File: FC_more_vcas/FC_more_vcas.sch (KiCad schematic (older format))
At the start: 33 parts, among them J1 Con_Bottom, J2 Con_Top, Q1 Q_PNP_EBC, Q2 Q_PNP_EBC, U1 LM13700

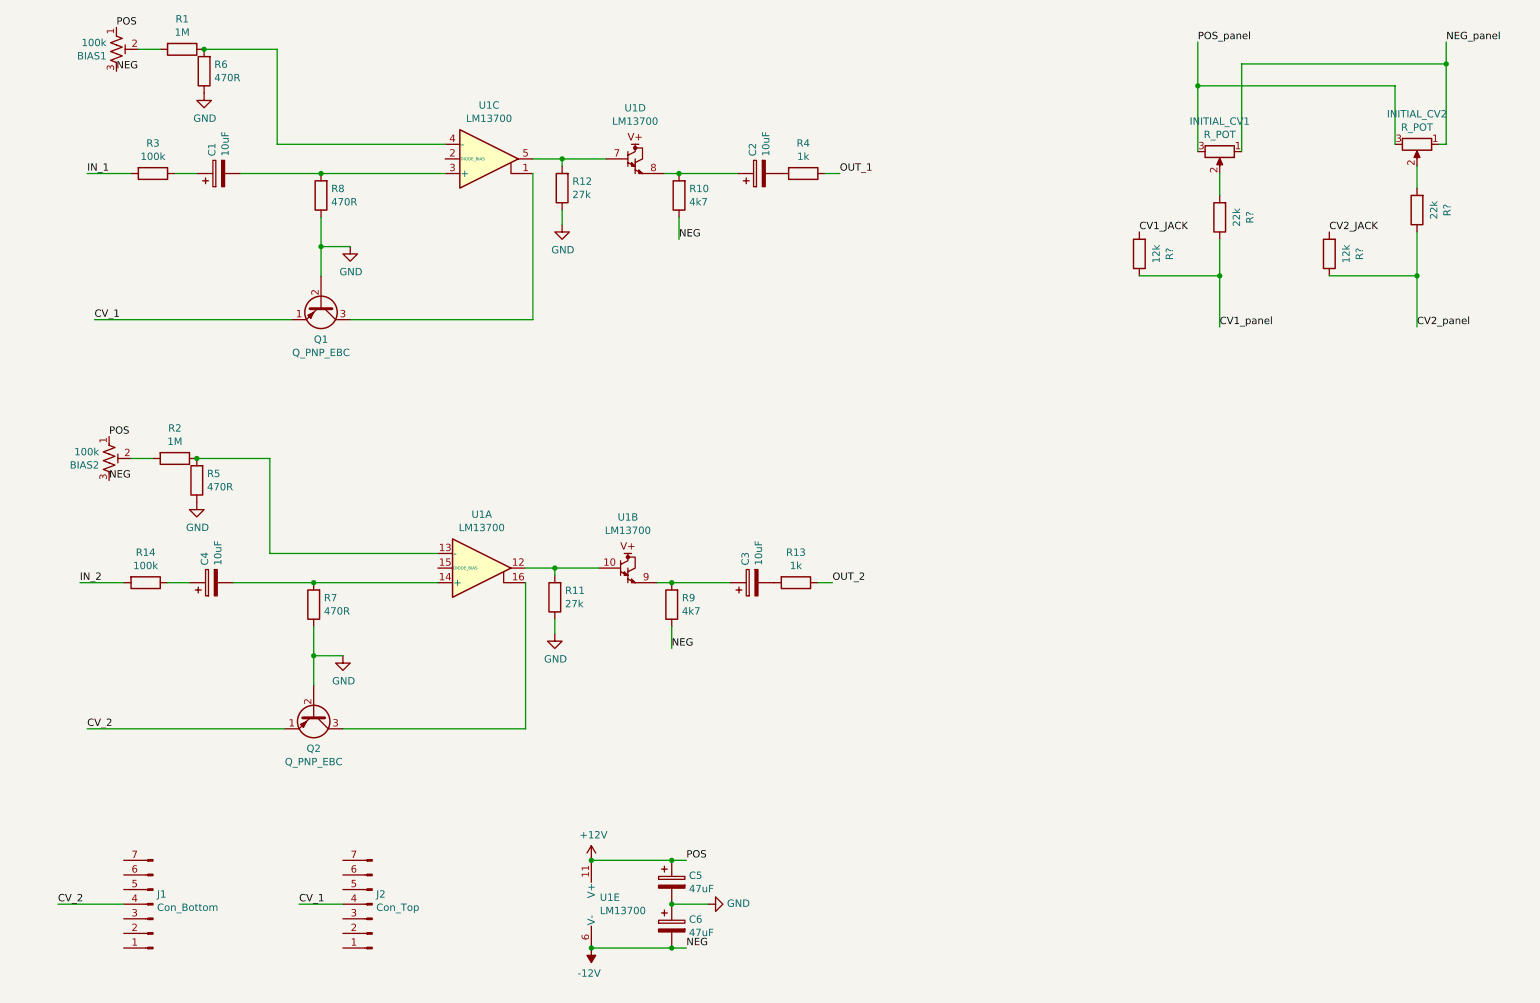
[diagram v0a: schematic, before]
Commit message: Yousynth ADSR layed out in Kicad, WASP reworked for more compact layout, FC more VCAs layed out
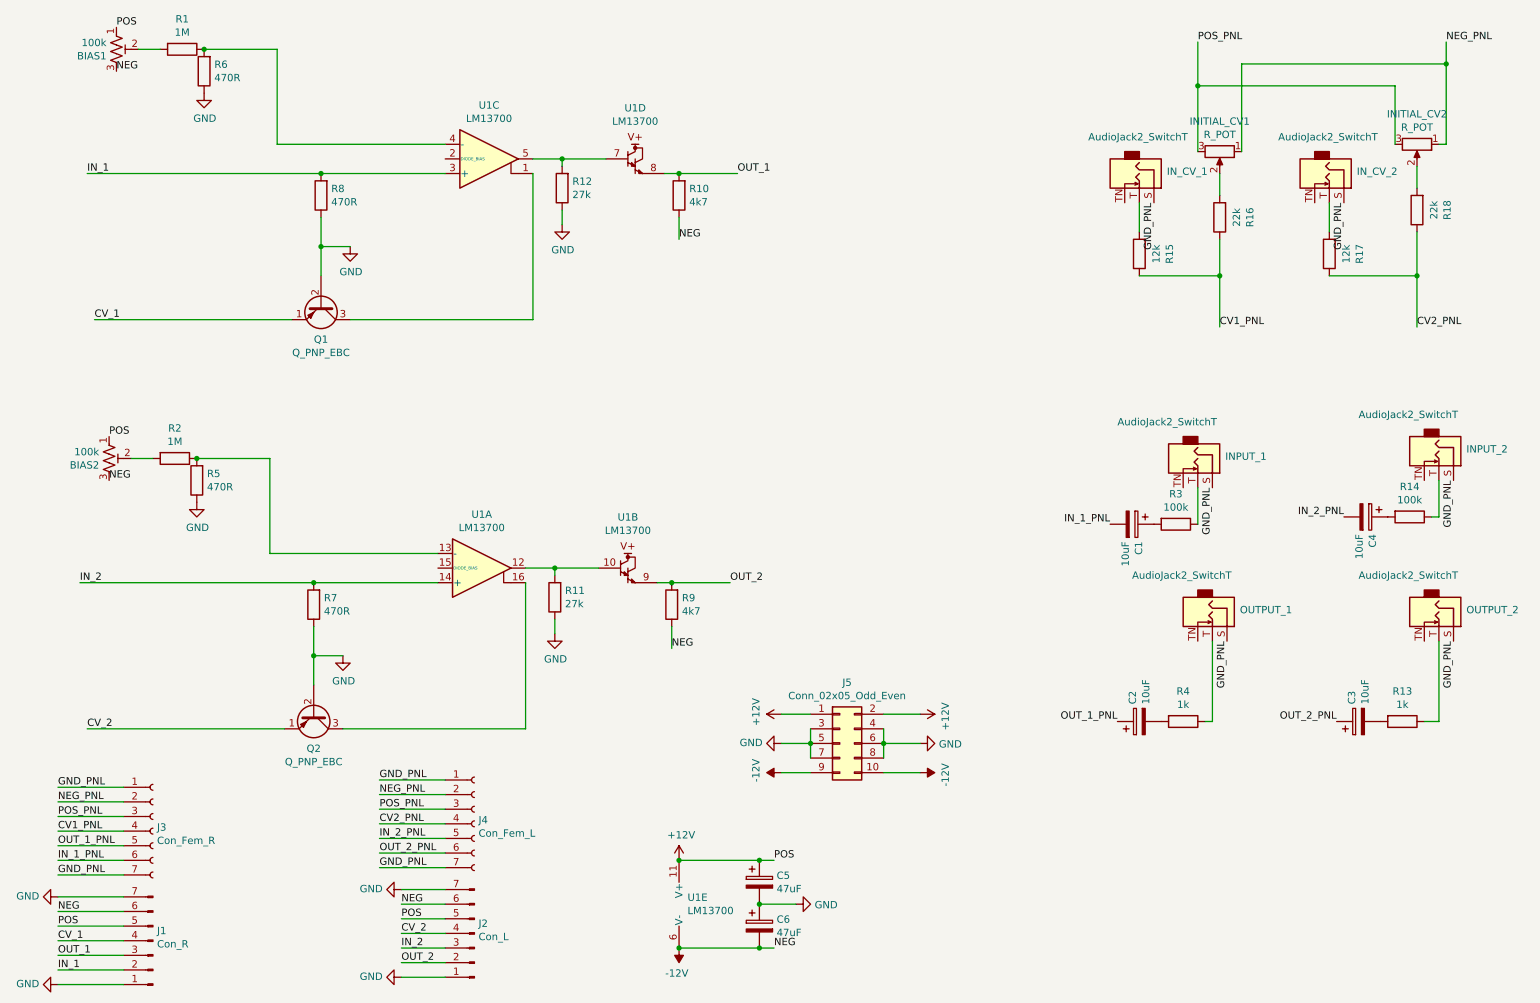
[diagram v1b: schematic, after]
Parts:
- added INPUT_1, INPUT_2, IN_CV_1, IN_CV_2, OUTPUT_1, OUTPUT_2: AudioJack2_SwitchT, Connector_Audio:Jack_3.5mm_QingPu_WQP-PJ398SM_Vertical_CircularHoles, symbol Connector:AudioJack2_SwitchT
- added J3: Con_Fem_R, Connector_PinSocket_2.54mm:PinSocket_1x07_P2.54mm_Vertical, symbol Connector:Conn_01x07_Female
- added J4: Con_Fem_L, Connector_PinSocket_2.54mm:PinSocket_1x07_P2.54mm_Vertical, symbol Connector:Conn_01x07_Female
- added J5: Conn_02x05_Odd_Even, Connector_PinHeader_2.54mm:PinHeader_2x05_P2.54mm_Vertical, symbol Connector_Generic:Conn_02x05_Odd_Even
- BIAS1, BIAS2: footprint (none) -> Potentiometer_THT:Potentiometer_Bourns_3296W_Vertical
- C1, C2, C3, C4: footprint (none) -> Capacitor_THT:CP_Radial_D5.0mm_P2.50mm
- C5, C6: footprint (none) -> Capacitor_THT:CP_Radial_D6.3mm_P2.50mm
- INITIAL_CV1, INITIAL_CV2: footprint (none) -> Potentiometer_THT:Potentiometer_Alpha_RD901F-40-00D_Single_Vertical
- J1: value Con_Bottom -> Con_R; footprint (none) -> Connector_PinHeader_2.54mm:PinHeader_1x07_P2.54mm_Vertical
- J2: value Con_Top -> Con_L; footprint (none) -> Connector_PinHeader_2.54mm:PinHeader_1x07_P2.54mm_Vertical
- Q1, Q2: footprint (none) -> Package_TO_SOT_SMD:SOT-23
- R1, R10, R11, R12, R13, R14, R2, R3, R4, R5, R6, R7, R8, R9: footprint (none) -> Resistor_SMD:R_0805_2012Metric_Pad1.15x1.40mm_HandSolder
- R15, R16, R17, R18: renamed from R?; footprint (none) -> Resistor_SMD:R_0805_2012Metric_Pad1.15x1.40mm_HandSolder
- U1: footprint (none) -> Package_DIP:DIP-16_W7.62mm_Socket_LongPads
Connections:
- net +12V: now also J1.5 (Pin_5), J2.5 (Pin_5), J5.1 (Pin_1), J5.2 (Pin_2)
- net -12V: now also J1.6 (Pin_6), J2.6 (Pin_6), J5.10 (Pin_10), J5.9 (Pin_9)
- net CV_1: now also J1.4 (Pin_4); no longer J2.4 (Pin_4)
- net CV_2: now also J2.4 (Pin_4); no longer J1.4 (Pin_4)
- net GND: now also J1.1 (Pin_1), J1.7 (Pin_7), J2.1 (Pin_1), J2.7 (Pin_7), J5.3 (Pin_3), J5.4 (Pin_4), J5.5 (Pin_5), J5.6 (Pin_6), J5.7 (Pin_7), J5.8 (Pin_8)
- net IN_1: now also J1.2 (Pin_2), R8.2, U1.3 (+); no longer R3.2
- net IN_2: now also J2.3 (Pin_3), R7.2, U1.14 (+); no longer R14.2
- net OUT_1: now also J1.3 (Pin_3), R10.2, U1.8; no longer R4.1
- net OUT_2: now also J2.2 (Pin_2), R9.2, U1.9; no longer R13.1
- net at R14.1: now also INPUT_2.T; no longer C4.1
- net at R3.1: now also INPUT_1.T; no longer C1.1
- net CV1_JACK: no longer names the net of R15.2
- net CV1_JACK: now also IN_CV_1.T
- net CV1_panel renamed CV1_PNL
- net CV1_PNL: now also J3.4 (Pin_4)
- net CV2_JACK: no longer names the net of R17.2
- net CV2_JACK: now also IN_CV_2.T
- net CV2_panel renamed CV2_PNL
- net CV2_PNL: now also J4.4 (Pin_4)
- net NEG_panel renamed NEG_PNL
- net NEG_PNL: now also J3.2 (Pin_2), J4.2 (Pin_2)
- net POS_panel renamed POS_PNL
- net POS_PNL: now also J3.3 (Pin_3), J4.3 (Pin_3)
- new net: C4.1, R14.2
- new net: OUTPUT_2.T, R13.1
- new net: C1.1, R3.2
- new net: OUTPUT_1.T, R4.1
- new net GND_PNL: INPUT_1.S, INPUT_2.S, IN_CV_1.S, IN_CV_2.S, J3.1 (Pin_1), J3.7 (Pin_7), J4.1 (Pin_1), J4.7 (Pin_7), OUTPUT_1.S, OUTPUT_2.S
- new net IN_1_PNL: C1.2, J3.6 (Pin_6)
- new net IN_2_PNL: C4.2, J4.5 (Pin_5)
- new net OUT_1_PNL: C2.1, J3.5 (Pin_5)
- new net OUT_2_PNL: C3.1, J4.6 (Pin_6)
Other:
- moved on the sheet: C1, C2, C3, C4, C5, C6, J1, J2, R13, R14, R3, R4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

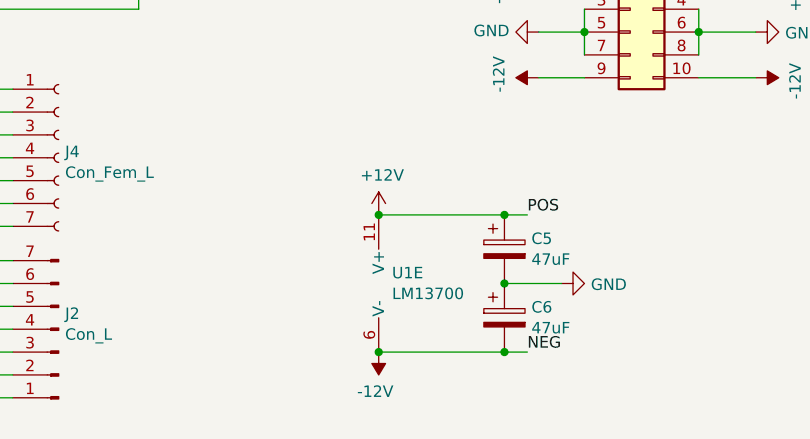
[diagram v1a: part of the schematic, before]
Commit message: Corrections made to ground planes, trace widths, etc. after visual checks of printout
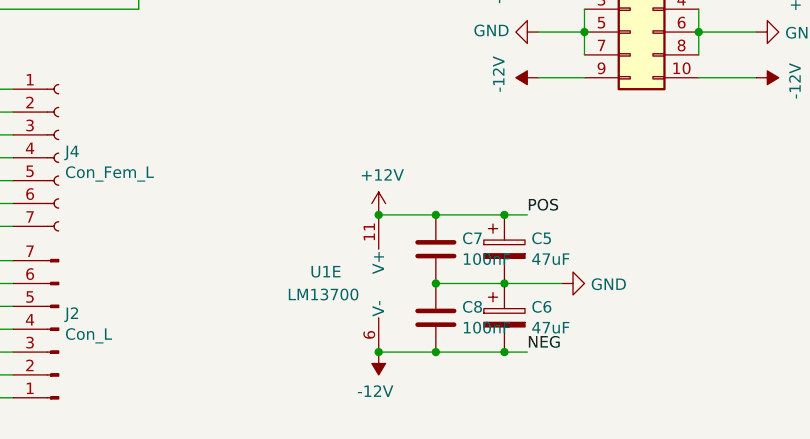
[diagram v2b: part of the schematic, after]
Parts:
- added C7, C8: 100nF, Capacitor_SMD:C_0805_2012Metric_Pad1.15x1.40mm_HandSolder, symbol Device:C
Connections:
- net +12V: now also C7.1
- net -12V: now also C8.2
- net GND: now also C7.2, C8.1
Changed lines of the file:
@@
 U 5 1 5E74031E
 P 5250 6950
-F 0 "U1" H 5208 6996 50  0000 L CNN
-F 1 "LM13700" H 5208 6905 50  0000 L CNN
+F 0 "U1" H 4850 7000 50  0000 L CNN
+F 1 "LM13700" H 4750 6900 50  0000 L CNN
 F 2 "Package_DIP:DIP-16_W7.62mm_Socket_LongPads" H 4950 6975 50  0001 C CNN
 F 3 "http://www.ti.com/lit/ds/symlink/lm13700.pdf" H 4950 6975 50  0001 C CNN
@@
 NEG
 Wire Wire Line
-	5150 7250 5700 7250
+	5150 7250 5400 7250
 Connection ~ 5150 7250
 Wire Wire Line
-	5150 6650 5700 6650
+	5150 6650 5400 6650
 Connection ~ 5150 6650
 Text Label 1050 4750 0    50   ~ 0
@@
 Wire Wire Line
 	10350 5700 10350 5150
+$Comp
+L Device:C C7
+U 1 1 5F15044E
+P 5400 6800
+F 0 "C7" H 5515 6846 50  0000 L CNN
+F 1 "100nF" H 5515 6755 50  0000 L CNN
+F 2 "Capacitor_SMD:C_0805_2012Metric_Pad1.15x1.40mm_HandSolder" H 5438 6650 50  0001 C CNN
+F 3 "~" H 5400 6800 50  0001 C CNN
+	1    5400 6800
+	1    0    0    -1
+$EndComp
+Connection ~ 5400 6650
+Wire Wire Line
+	5400 6650 5700 6650
+$Comp
+L Device:C C8
+U 1 1 5F151C78
+P 5400 7100
+F 0 "C8" H 5515 7146 50  0000 L CNN
+F 1 "100nF" H 5515 7055 50  0000 L CNN
+F 2 "Capacitor_SMD:C_0805_2012Metric_Pad1.15x1.40mm_HandSolder" H 5438 6950 50  0001 C CNN
+F 3 "~" H 5400 7100 50  0001 C CNN
+	1    5400 7100
+	1    0    0    -1
+$EndComp
+Connection ~ 5400 7250
+Wire Wire Line
+	5400 7250 5700 7250
+Wire Wire Line
+	5400 6950 5700 6950
+Connection ~ 5400 6950
 $EndSCHEMATC
